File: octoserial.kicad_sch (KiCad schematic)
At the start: 46 parts, among them J1 USB_OTG

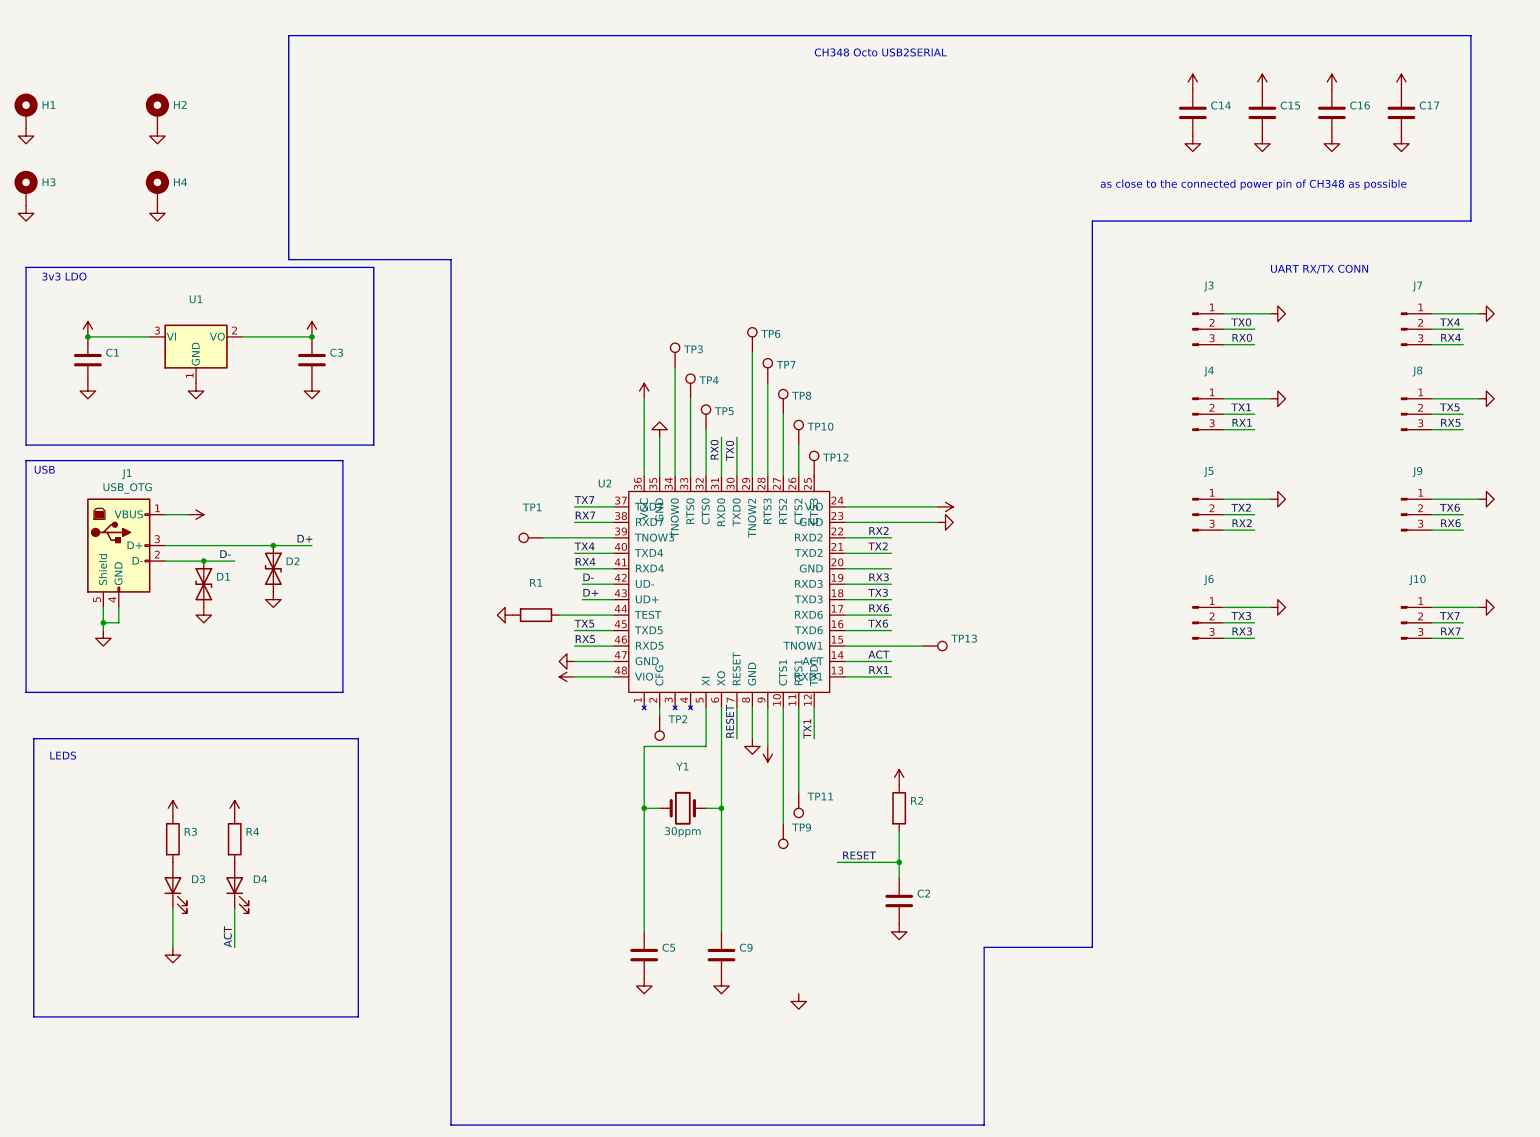
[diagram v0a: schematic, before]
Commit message: Add gpio/3.3 headers
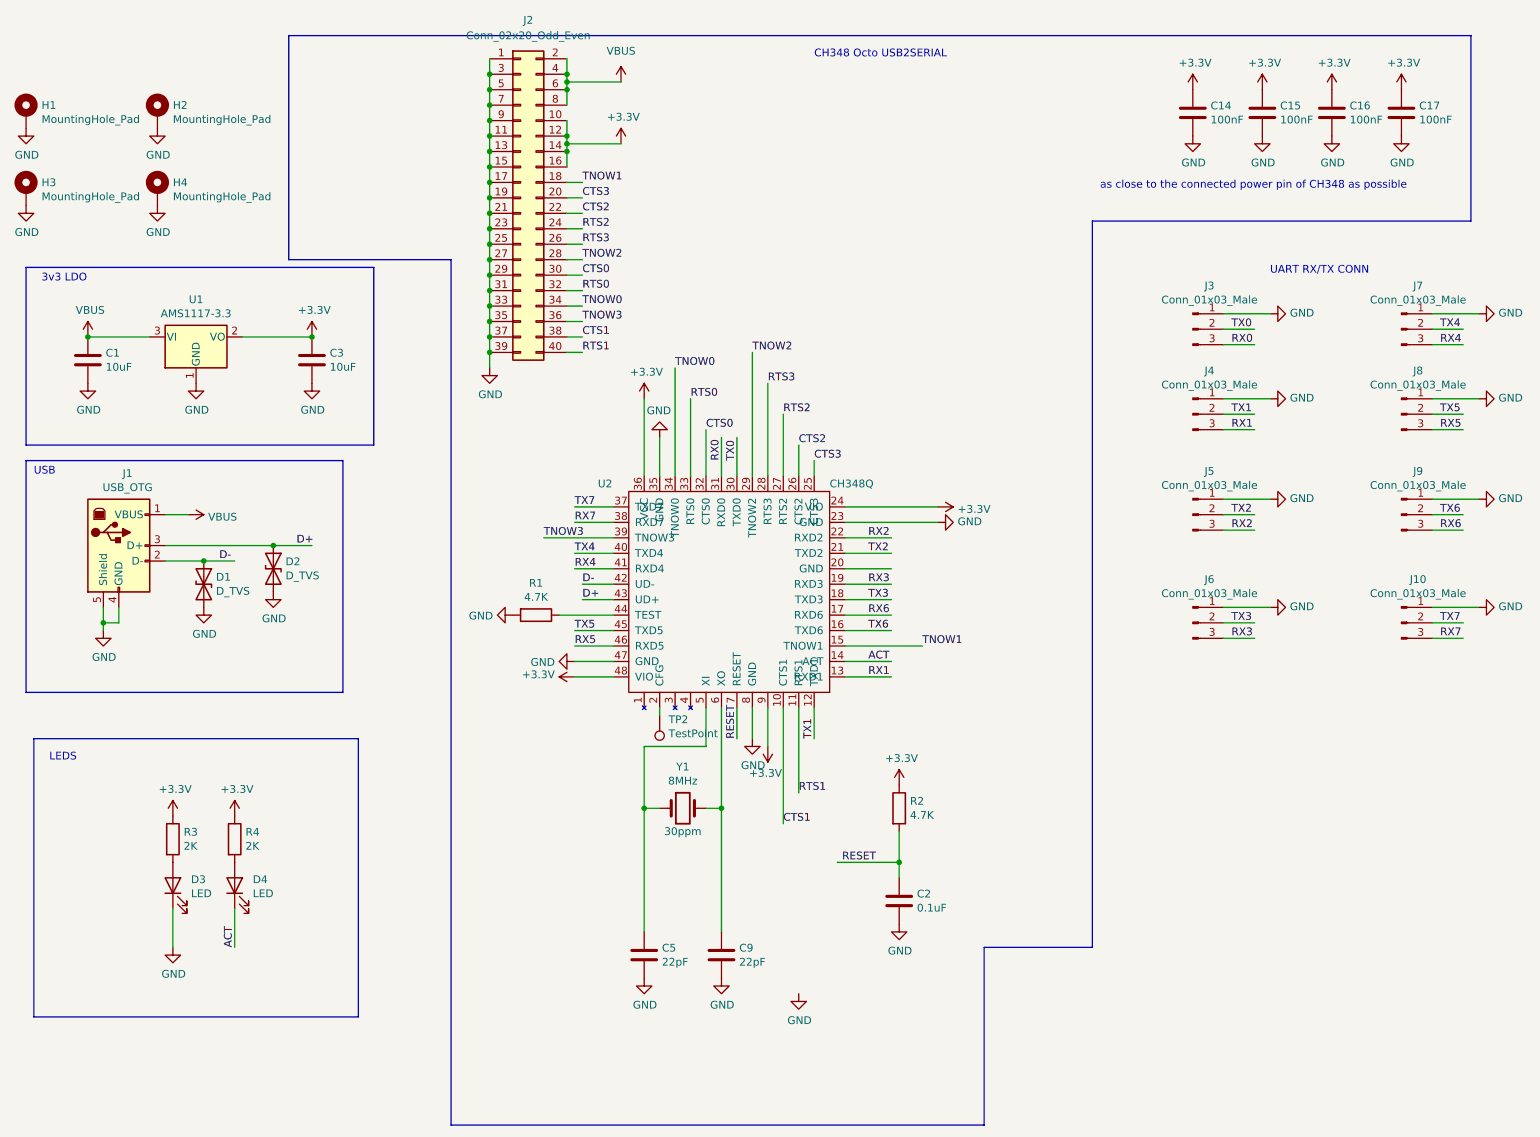
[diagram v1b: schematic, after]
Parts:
- removed TP1, TP10, TP11, TP12, TP13, TP3, TP4, TP5, TP6, TP7, TP8, TP9: (no value), symbol Connector:TestPoint
- added J2: Conn_02x20_Odd_Even, Connector_PinHeader_2.54mm:PinHeader_2x20_P2.54mm_Vertical, symbol Connector_Generic:Conn_02x20_Odd_Even
- C1, C3: value (none) -> 10uF
- C14, C15, C16, C17: value (none) -> 100nF
- C2: value (none) -> 0.1uF
- C5, C9: value (none) -> 22pF
- D1, D2: value (none) -> D_TVS; footprint (none) -> Diode_SMD:D_0603_1608Metric_Pad1.05x0.95mm_HandSolder; now left out of the parts list
- D3, D4: value (none) -> LED; footprint (none) -> LED_SMD:LED_1206_3216Metric_Pad1.42x1.75mm_HandSolder
- H1, H2, H3, H4: value (none) -> MountingHole_Pad; footprint (none) -> MountingHole:MountingHole_3.2mm_M3_Pad
- J10, J3, J4, J5, J6, J7, J8, J9: value (none) -> Conn_01x03_Male; footprint (none) -> Connector_PinSocket_2.54mm:PinSocket_1x03_P2.54mm_Horizontal
- R1, R2: value (none) -> 4.7K
- R3, R4: value (none) -> 2K
- TP2: value (none) -> TestPoint; footprint (none) -> TestPoint:TestPoint_Pad_D1.0mm
- U1: value (none) -> AMS1117-3.3
- U2: value (none) -> CH348Q; footprint (none) -> Package_QFP:LQFP-48_7x7mm_P0.5mm
- Y1: value (none) -> 8MHz; footprint (none) -> Crystal:Crystal_HC49-4H_Vertical
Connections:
- net +3V3: now also J2.10 (Pin_10), J2.12 (Pin_12), J2.14 (Pin_14), J2.16 (Pin_16)
- net GND: now also J2.1 (Pin_1), J2.11 (Pin_11), J2.13 (Pin_13), J2.15 (Pin_15), J2.17 (Pin_17), J2.19 (Pin_19), J2.21 (Pin_21), J2.23 (Pin_23), J2.25 (Pin_25), J2.27 (Pin_27), J2.29 (Pin_29), J2.3 (Pin_3), J2.31 (Pin_31), J2.33 (Pin_33), J2.35 (Pin_35), J2.37 (Pin_37), J2.39 (Pin_39), J2.5 (Pin_5), J2.7 (Pin_7), J2.9 (Pin_9)
- net VBUS: now also J2.2 (Pin_2), J2.4 (Pin_4), J2.6 (Pin_6), J2.8 (Pin_8)
- net CTS1: now reaches U2.10 (CTS1)
- net CTS1: now also J2.38 (Pin_38)
- net RTS1: now reaches U2.11 (RTS1)
- net RTS1: now also J2.40 (Pin_40)
- net TNOW1: now reaches U2.15 (TNOW1)
- net TNOW1: now also J2.18 (Pin_18)
- net CTS3: now reaches U2.25 (CTS3)
- net CTS3: now also J2.20 (Pin_20)
- net CTS2: now reaches U2.26 (CTS2)
- net CTS2: now also J2.22 (Pin_22)
- net RTS2: now reaches U2.27 (RTS2)
- net RTS2: now also J2.24 (Pin_24)
- net RTS3: now reaches U2.28 (RTS3)
- net RTS3: now also J2.26 (Pin_26)
- net TNOW2: now reaches U2.29 (TNOW2)
- net TNOW2: now also J2.28 (Pin_28)
- net CTS0: now reaches U2.32 (CTS0)
- net CTS0: now also J2.30 (Pin_30)
- net RTS0: now reaches U2.33 (RTS0)
- net RTS0: now also J2.32 (Pin_32)
- net TNOW0: now reaches U2.34 (TNOW0)
- net TNOW0: now also J2.34 (Pin_34)
- net TNOW3: now reaches U2.39 (TNOW3)
- net TNOW3: now also J2.36 (Pin_36)

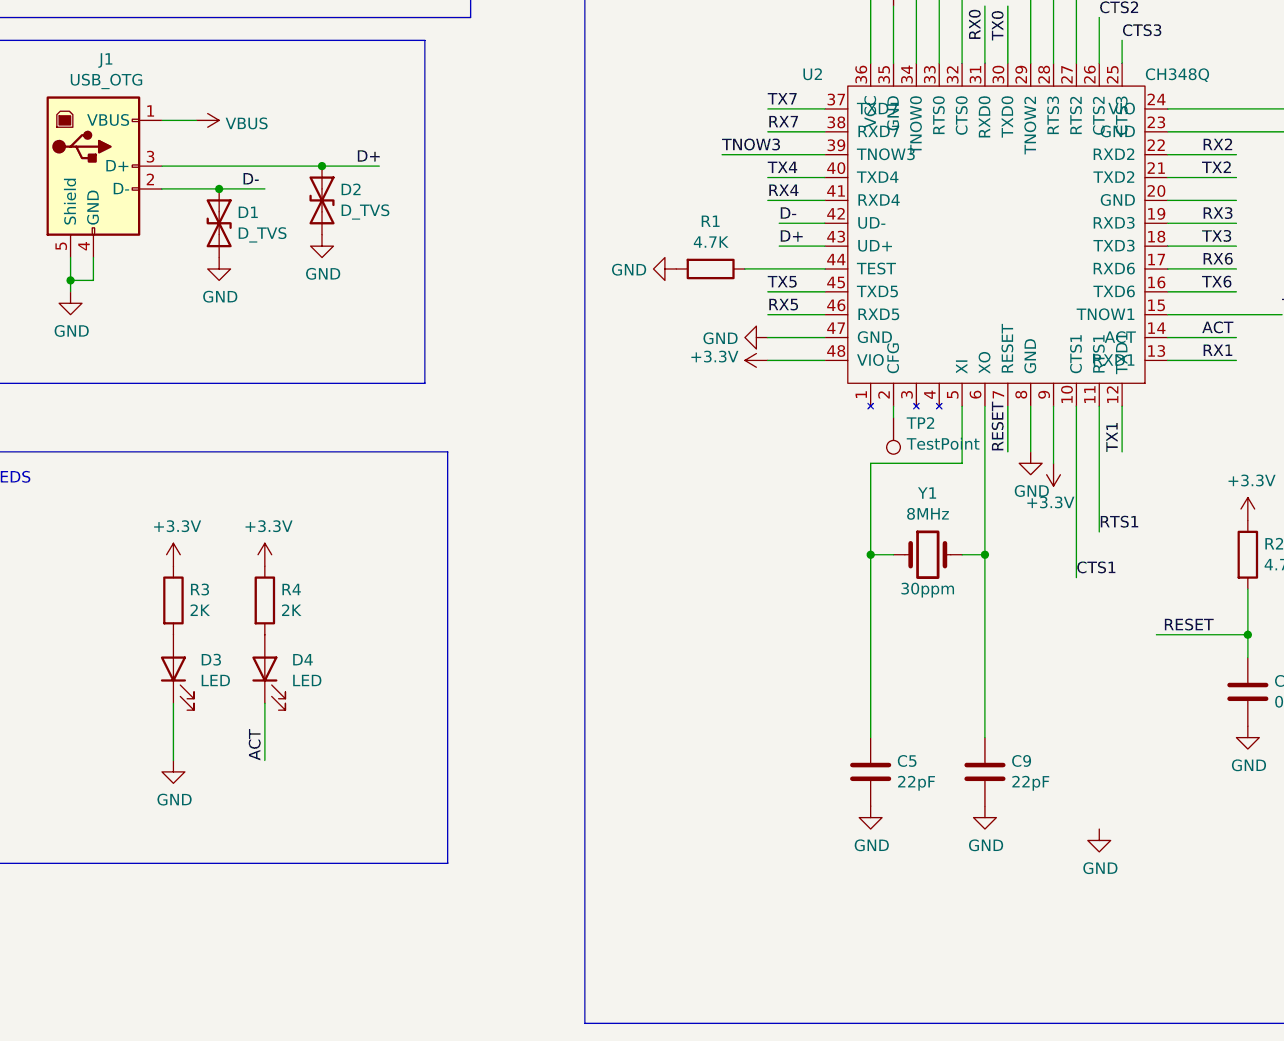
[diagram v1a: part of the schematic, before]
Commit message: Add JPC & LCSC tags & regenerate gerber + bom CSVs
Signed-off-by: Neil Armstrong <neil.armstrong@linaro.org>
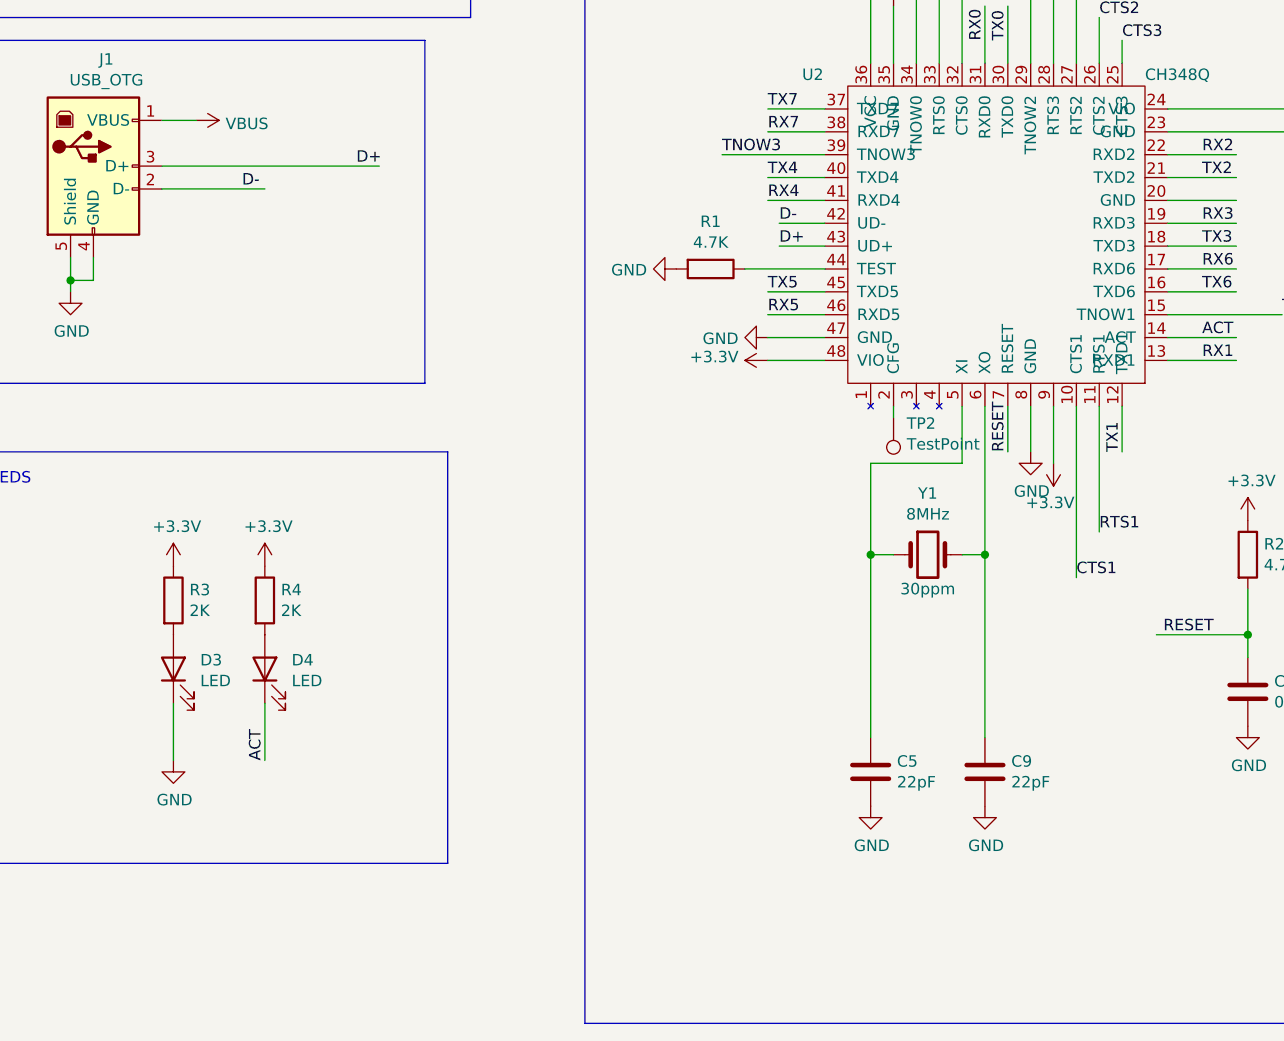
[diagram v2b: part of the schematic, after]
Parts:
- removed D1, D2: D_TVS, Diode_SMD:D_0603_1608Metric_Pad1.05x0.95mm_HandSolder, symbol Device:D_TVS
- C1, C3: JLC (none) -> 1206; LCSC (none) -> C13585
- C14, C15, C16, C17, C2: JLC (none) -> 1206; LCSC (none) -> C110255
- C5, C9: JLC (none) -> 1206; LCSC (none) -> C5137630
- D3: JLC (none) -> 1206; LCLSC (none) -> C434438
- D4: JLC (none) -> 1206; LCSC (none) -> C434438
- J1: LCSC (none) -> C46392
- J10, J3, J4, J5, J6, J7, J8, J9: LCSC (none) -> C5116482
- J2: LCSC (none) -> C124383
- R1, R2: JLC (none) -> 1206; LCSC (none) -> C17936
- R3, R4: JLC (none) -> 1206; LCSC (none) -> C17944
- U1: JLC (none) -> SOT-223-3; LCSC (none) -> C173386
- U2: LCSC (none) -> C2979161
- Y1: LCSC (none) -> C21263
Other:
- company: (none) -> https://github.com/superna9999/octoserial
